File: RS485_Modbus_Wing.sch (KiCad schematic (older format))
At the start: 13 parts, among them J1 feather long, J2 feather short, J3 Screw_Terminal_01x02, U1 SP3485EN

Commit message: Add_BOM
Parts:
- C1: manf# (none) -> CC0603KRX5R6BB106
- C2: manf# (none) -> 0603F104Z160CT
- R1, R2, R3, R4: manf# (none) -> RC0603JR-0710KL
- R5, R7: manf# (none) -> 0603WAJ0203T5E
- R6: manf# (none) -> RTT03121JTP
- U1: manf# (none) -> SP3485CN
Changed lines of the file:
@@
 F 1 "SP3485EN" H 4160 2500 50  0000 C CNN
 F 2 "Package_SO:SOIC-8_3.9x4.9mm_P1.27mm" H 5500 1770 50  0001 C CIN
-F 3 "https://www.mouser.mx/datasheet/2/146/sp3485-1816391.pdf" H 4450 2120 50  0001 C CNN
+F 3 "https://www.mouser.mx/ProductDetail/MaxLinear/SP3485CN-L-TR?qs=3EMgrMjM0fZL2ArUMUL9Gg%3D%3D" H 4450 2120 50  0001 C CNN
+F 4 "SP3485CN" H 4450 2120 50  0001 C CNN "manf#"
 	1    4450 2120
 	1    0    0    -1
@@
 F 1 "10K" V 3740 1500 50  0000 L CNN
 F 2 "Resistor_SMD:R_0603_1608Metric_Pad1.05x0.95mm_HandSolder" H 3810 1570 50  0001 C CNN
-F 3 "~" H 3810 1570 50  0001 C CNN
+F 3 "https://lcsc.com/product-detail/Chip-Resistor-Surface-Mount_10KR-103-5_C99198.html" H 3810 1570 50  0001 C CNN
+F 4 "RC0603JR-0710KL" H 3810 1570 50  0001 C CNN "manf#"
 	1    3810 1570
 	1    0    0    -1
@@
 F 1 "10K" V 3540 1500 50  0000 L CNN
 F 2 "Resistor_SMD:R_0603_1608Metric_Pad1.05x0.95mm_HandSolder" H 3600 1570 50  0001 C CNN
-F 3 "~" H 3600 1570 50  0001 C CNN
+F 3 "https://lcsc.com/product-detail/Chip-Resistor-Surface-Mount_10KR-103-5_C99198.html" H 3600 1570 50  0001 C CNN
+F 4 "RC0603JR-0710KL" H 3600 1570 50  0001 C CNN "manf#"
 	1    3600 1570
 	1    0    0    -1
@@
 F 1 "10K" V 3320 1510 50  0000 L CNN
 F 2 "Resistor_SMD:R_0603_1608Metric_Pad1.05x0.95mm_HandSolder" H 3390 1570 50  0001 C CNN
-F 3 "~" H 3390 1570 50  0001 C CNN
+F 3 "https://lcsc.com/product-detail/Chip-Resistor-Surface-Mount_10KR-103-5_C99198.html" H 3390 1570 50  0001 C CNN
+F 4 "RC0603JR-0710KL" H 3390 1570 50  0001 C CNN "manf#"
 	1    3390 1570
 	1    0    0    -1
@@
 F 1 "10K" V 3090 1490 50  0000 L CNN
 F 2 "Resistor_SMD:R_0603_1608Metric_Pad1.05x0.95mm_HandSolder" H 3180 1570 50  0001 C CNN
-F 3 "~" H 3180 1570 50  0001 C CNN
+F 3 "https://lcsc.com/product-detail/Chip-Resistor-Surface-Mount_10KR-103-5_C99198.html" H 3180 1570 50  0001 C CNN
+F 4 "RC0603JR-0710KL" H 3180 1570 50  0001 C CNN "manf#"
 	1    3180 1570
 	1    0    0    -1
@@
 F 1 "20K" V 7000 1750 50  0000 L CNN
 F 2 "Resistor_SMD:R_0603_1608Metric_Pad1.05x0.95mm_HandSolder" H 7070 1820 50  0001 C CNN
-F 3 "~" H 7070 1820 50  0001 C CNN
+F 3 "https://lcsc.com/product-detail/Chip-Resistor-Surface-Mount_UNI-ROYAL-Uniroyal-Elec-0603WAJ0203T5E_C25586.html" H 7070 1820 50  0001 C CNN
+F 4 "0603WAJ0203T5E" H 7070 1820 50  0001 C CNN "manf#"
 	1    7070 1820
 	1    0    0    -1
@@
 F 1 "120" V 7070 2060 50  0000 L CNN
 F 2 "Resistor_SMD:R_0603_1608Metric_Pad1.05x0.95mm_HandSolder" H 7140 2130 50  0001 C CNN
-F 3 "~" H 7140 2130 50  0001 C CNN
+F 3 "https://lcsc.com/product-detail/Chip-Resistor-Surface-Mount_120R-121-5_C103256.html" H 7140 2130 50  0001 C CNN
+F 4 "RTT03121JTP" H 7140 2130 50  0001 C CNN "manf#"
 	1    7140 2130
 	1    0    0    -1
@@
 F 1 "10uF" H 5312 2835 50  0000 L CNN
 F 2 "Capacitor_SMD:C_0603_1608Metric_Pad1.05x0.95mm_HandSolder" H 5220 2880 50  0001 C CNN
-F 3 "~" H 5220 2880 50  0001 C CNN
+F 3 "https://lcsc.com/product-detail/Others_YAGEO-CC0603KRX5R6BB106_C326057.html" H 5220 2880 50  0001 C CNN
+F 4 "CC0603KRX5R6BB106" H 5220 2880 50  0001 C CNN "manf#"
 	1    5220 2880
 	1    0    0    -1
@@
 F 1 "0.1uF" H 5732 2845 50  0000 L CNN
 F 2 "Capacitor_SMD:C_0603_1608Metric_Pad1.05x0.95mm_HandSolder" H 5640 2890 50  0001 C CNN
-F 3 "~" H 5640 2890 50  0001 C CNN
+F 3 "https://lcsc.com/product-detail/Multilayer-Ceramic-Capacitors-MLCC-SMD-SMT_Walsin-Tech-Corp-0603F104Z160CT_C387984.html" H 5640 2890 50  0001 C CNN
+F 4 "0603F104Z160CT" H 5640 2890 50  0001 C CNN "manf#"
 	1    5640 2890
 	1    0    0    -1
@@
 F 1 "20K" V 7000 2330 50  0000 L CNN
 F 2 "Resistor_SMD:R_0603_1608Metric_Pad1.05x0.95mm_HandSolder" H 7070 2400 50  0001 C CNN
-F 3 "~" H 7070 2400 50  0001 C CNN
+F 3 "https://lcsc.com/product-detail/Chip-Resistor-Surface-Mount_UNI-ROYAL-Uniroyal-Elec-0603WAJ0203T5E_C25586.html" H 7070 2400 50  0001 C CNN
+F 4 "0603WAJ0203T5E" H 7070 2400 50  0001 C CNN "manf#"
 	1    7070 2400
 	1    0    0    -1

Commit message: Add_item
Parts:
- J3: manf# (none) -> WJ500V-5.08-2P
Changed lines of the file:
@@
 F 1 "Screw_Terminal_01x02" H 7490 1941 50  0000 L CNN
 F 2 "TerminalBlock:TerminalBlock_bornier-2_P5.08mm" H 7410 2040 50  0001 C CNN
-F 3 "~" H 7410 2040 50  0001 C CNN
+F 3 "https://lcsc.com/product-detail/Pluggable-System-Terminal-Block_Ningbo-Kangnex-Elec-WJ500V-5-08-2P-14-00A_C8465.html" H 7410 2040 50  0001 C CNN
+F 4 "WJ500V-5.08-2P" H 7410 2040 50  0001 C CNN "manf#"
 	1    7410 2040
 	1    0    0    -1

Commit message: Change_conection
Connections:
- net RX is gone; now on net RO: J1.3 (Pin_3)
- net TX is gone; now on net DI: J1.2 (Pin_2)
- net DI: no longer J2.8 (Pin_8)
- net RO: no longer J2.5 (Pin_5)
- new net D12: J2.8 (Pin_8)
- new net D9: J2.5 (Pin_5)
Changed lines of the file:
@@
 MISO
 Text Label 8700 2200 0    50   ~ 0
-RX
-Text Label 8700 2300 0    50   ~ 0
-TX
+RO
 Text Label 8700 2400 0    50   ~ 0
 FREE
@@
 Text Label 9950 1600 2    50   ~ 0
 D13
-Text Label 9950 1700 2    50   ~ 0
-DI
 Text Label 9950 1800 2    50   ~ 0
 DE
-Text Label 9950 1900 2    50   ~ 0
-RE
-Text Label 9950 2000 2    50   ~ 0
-RO
-Text Label 9950 2300 2    50   ~ 0
-SCL
-Text Label 9950 2400 2    50   ~ 0
-SDA
 Wire Wire Line
 	8700 900  8900 900
@@
 	9700 1600 9950 1600
 Wire Wire Line
-	9700 1700 9950 1700
-Wire Wire Line
 	9700 1800 9950 1800
 Wire Wire Line
-	9700 1900 9950 1900
-Wire Wire Line
 	9700 2000 9950 2000
-Wire Wire Line
-	9700 2100 9950 2100
-Wire Wire Line
-	9700 2200 9950 2200
-Wire Wire Line
-	9700 2300 9950 2300
-Wire Wire Line
-	9700 2400 9950 2400
 $Comp
 L power:+3.3V #PWR0114
@@
 Text Notes 8480 590  0    50   ~ 0
 PINS
-Text Label 9950 2100 2    50   ~ 0
-D6
-Text Label 9950 2200 2    50   ~ 0
-D5
 $Comp
 L Interface_UART:SP3485EN U1
@@
 	1    0    0    -1
 $EndComp
+Wire Wire Line
+	9700 2400 9950 2400
+Text Label 9950 2400 2    50   ~ 0
+SDA
+Wire Wire Line
+	9700 2300 9950 2300
+Text Label 9950 2300 2    50   ~ 0
+SCL
+Text Label 9950 2200 2    50   ~ 0
+D5
+Wire Wire Line
+	9700 2200 9950 2200
+Wire Wire Line
+	9700 2100 9950 2100
+Text Label 9950 2100 2    50   ~ 0
+D6
+Wire Wire Line
+	9700 1700 9950 1700
+Wire Wire Line
+	9700 1900 9950 1900
+Text Label 9950 1900 2    50   ~ 0
+RE
+Text Label 8700 2300 0    50   ~ 0
+DI
+Text Label 9950 1700 2    50   ~ 0
+D12
+Text Label 9950 2000 2    50   ~ 0
+D9
 $EndSCHEMATC

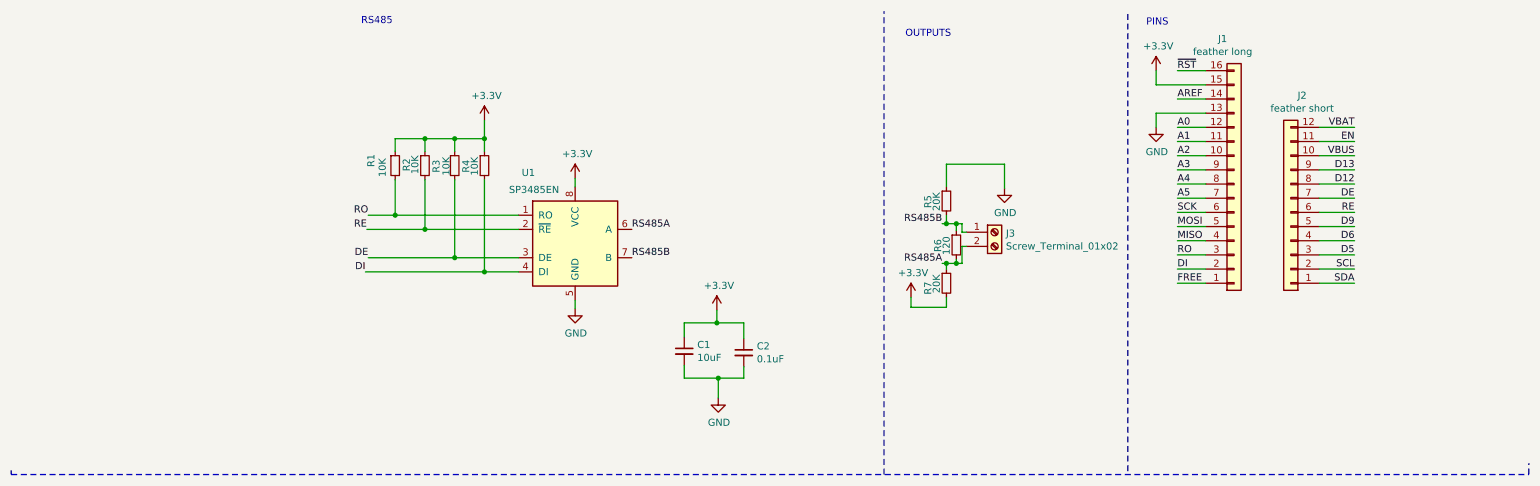
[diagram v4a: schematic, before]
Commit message: Change_labels
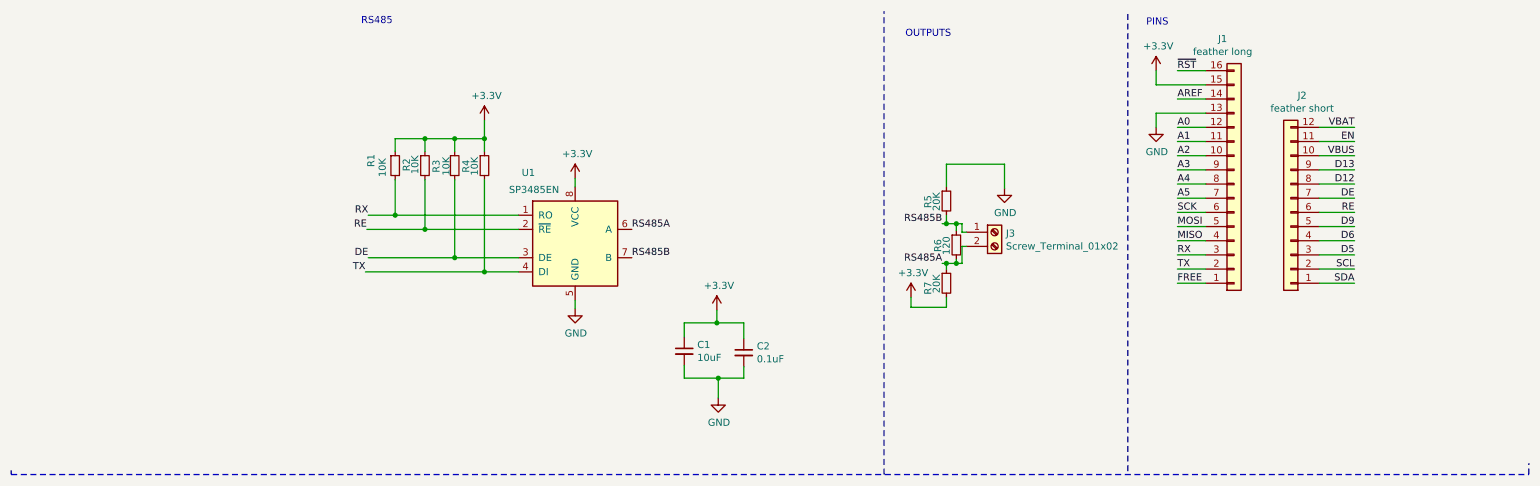
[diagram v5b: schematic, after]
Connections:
- net DI renamed TX
- net RO renamed RX
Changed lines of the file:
@@
 MISO
 Text Label 8700 2200 0    50   ~ 0
-RO
+RX
 Text Label 8700 2400 0    50   ~ 0
 FREE
@@
 RE
 Text Label 2990 1920 2    50   ~ 0
-RO
+RX
 Text Label 2990 2220 2    50   ~ 0
 DE
 Text Label 2970 2320 2    50   ~ 0
-DI
+TX
 Wire Wire Line
 	2990 1920 3180 1920
@@
 RE
 Text Label 8700 2300 0    50   ~ 0
-DI
+TX
 Text Label 9950 1700 2    50   ~ 0
 D12
